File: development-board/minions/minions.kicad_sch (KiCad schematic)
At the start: 101 parts, among them J1 Pinout, J2 SWD_JLINK, J3 0.91 OLED, J4 BatCon, J5 Pinout, K1 KEYSW, K2 KEYSW, K3 KEYSW, K4 KEYSW, K5 KEYSW, K6 KEYSW, K7 KEYSW, K8 KEYSW, P1 USB_C_Plug_USB2.0, Q1 PJA3404_(G1,D3,S2), Q2 PJA3405_(G1,D3,S2), SW1 RST, SW3 PWR_SWITCH, SW4 5V_EN, U10 MAX17048, U4 CH340C, U5 BQ24075RGT_DPPM, U6 TPS63002_SEPIC_5V, U7 nRF52832-QFxx, U8 MCP23017_SS, U9 TPS63001_SEPIC_3V3, Y1 32MHz_CF4032M00020001

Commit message: feat: routing minions part 1
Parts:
- removed J4: BatCon, Connector_PinHeader_2.54mm:PinHeader_1x02_P2.54mm_Horizontal, symbol Connector_Generic:Conn_01x02
- added C10: 1uF, Capacitor_SMD:C_0805_2012Metric_Pad1.18x1.45mm_HandSolder, symbol Device:C
- added C22: 0.1uF, Capacitor_SMD:C_0805_2012Metric_Pad1.18x1.45mm_HandSolder, symbol Device:C
- added J6: ConnBattery, Connector_PinHeader_2.54mm:PinHeader_1x03_P2.54mm_Horizontal, symbol Connector_Generic:Conn_01x03
- added SW2: SW_RGB, Button_Switch_SMD:SW_SPDT_PCM12, symbol Switch:SW_Push_SPDT
- added U1: SN74LV1T34DBV, Package_TO_SOT_SMD:SOT-23-5_HandSoldering, symbol Logic_LevelTranslator:SN74LV1T34DBV
- R15, R17: value 1K -> 1K5
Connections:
- net P0.24 is gone; now on net ~{PGOOD}: J1.1 (Pin_1), U7.29 (P0.24)
- net P0.25 is gone; now on net ~{CHG}: J1.2 (Pin_2), U7.37 (P0.25)
- net P0.26 is gone; now on net ~{ALRT}: J1.3 (Pin_3), U7.38 (P0.26)
- net +5V: now also SW2.1 (A); no longer C41.1, C42.1, C43.1, C44.1, D11.4 (VDD), D17.4 (VDD), D23.4 (VDD), D8.4 (VDD)
- net +BATT: now also C22.1, J6.1 (Pin_1)
- net GND: now also C10.2, C22.2, J6.3 (Pin_3), U1.3 (GND)
- net TX: now also U1.2 (A); no longer D8.3 (DIN)
- net VBUS: now also C10.1
- net TS: now reaches U5.1 (TS)
- net TS: now also J6.2 (Pin_2)
- net ~{PGOOD}: now reaches D4.1 (K), U5.7 (~{PGOOD})
- net ~{CHG}: now reaches D32.1 (K), U5.9 (~{CHG})
- net ~{ALRT}: now reaches U10.5 (~{ALRT})
- new net: C41.1, C42.1, C43.1, C44.1, D11.4 (VDD), D17.4 (VDD), D23.4 (VDD), D8.4 (VDD), SW2.2 (B), U1.5 (VCC)
- new net: D8.3 (DIN), U1.4 (Y)
- no-connect marks 29 -> 28
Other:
- note added: "dynamic power path management"
- moved on the sheet: C1, C11, C12, C13, C14, C15, C16, C17, C2, C3, C4, C41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

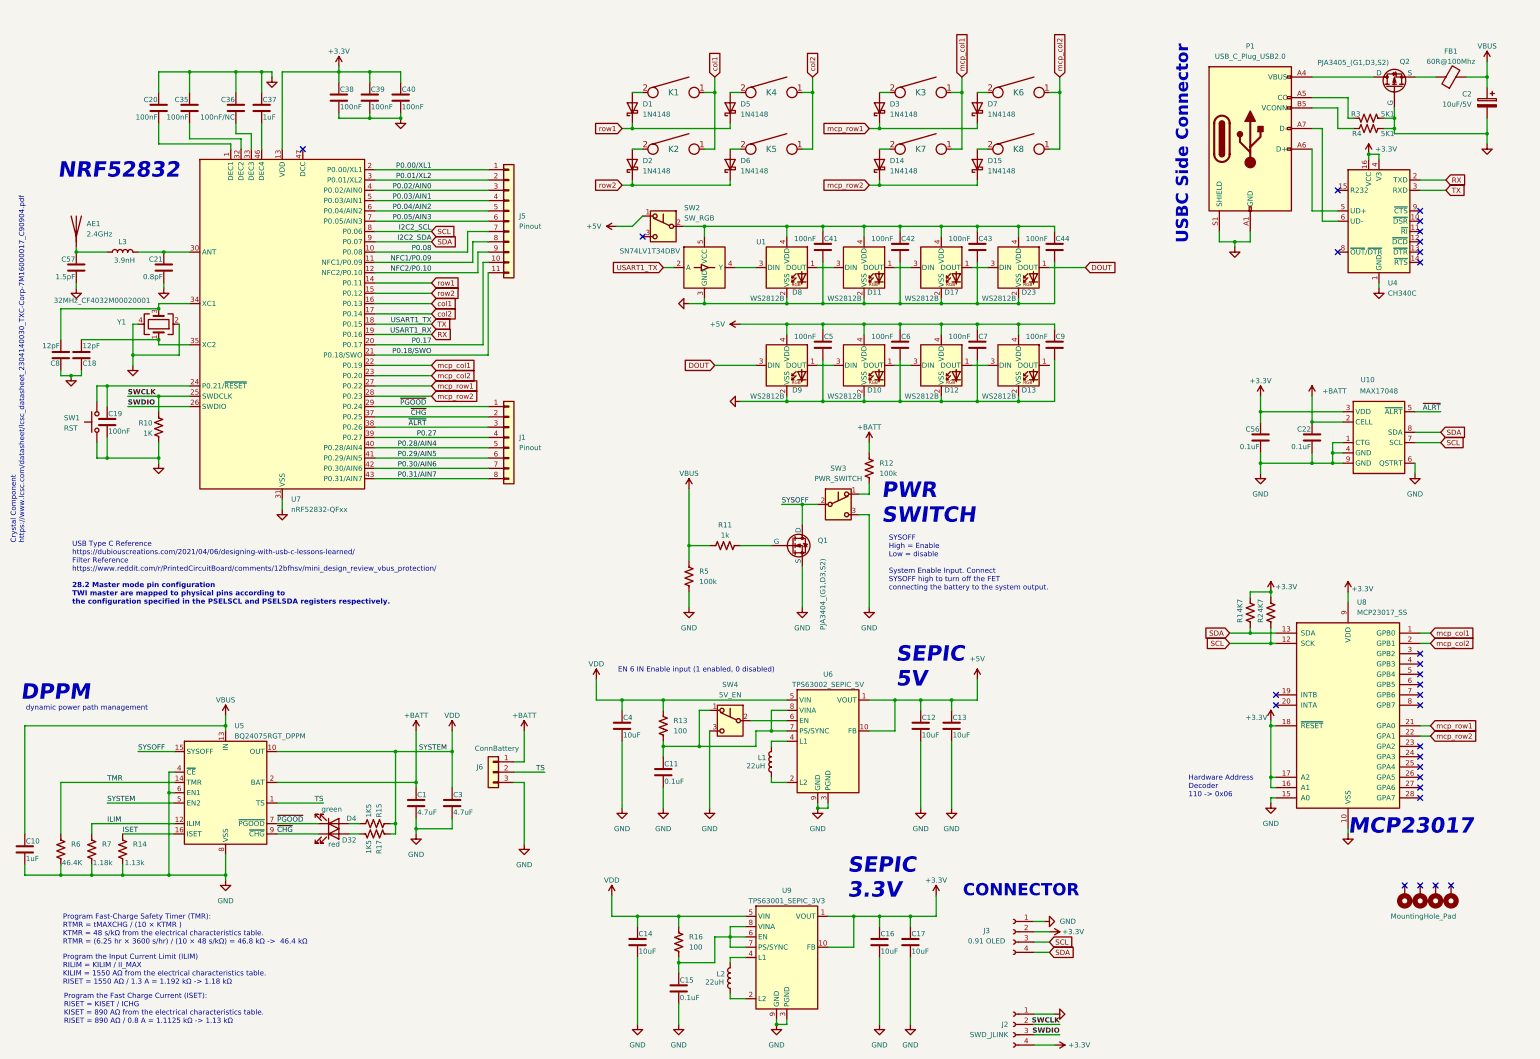
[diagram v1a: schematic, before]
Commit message: feat: finish routing part 1
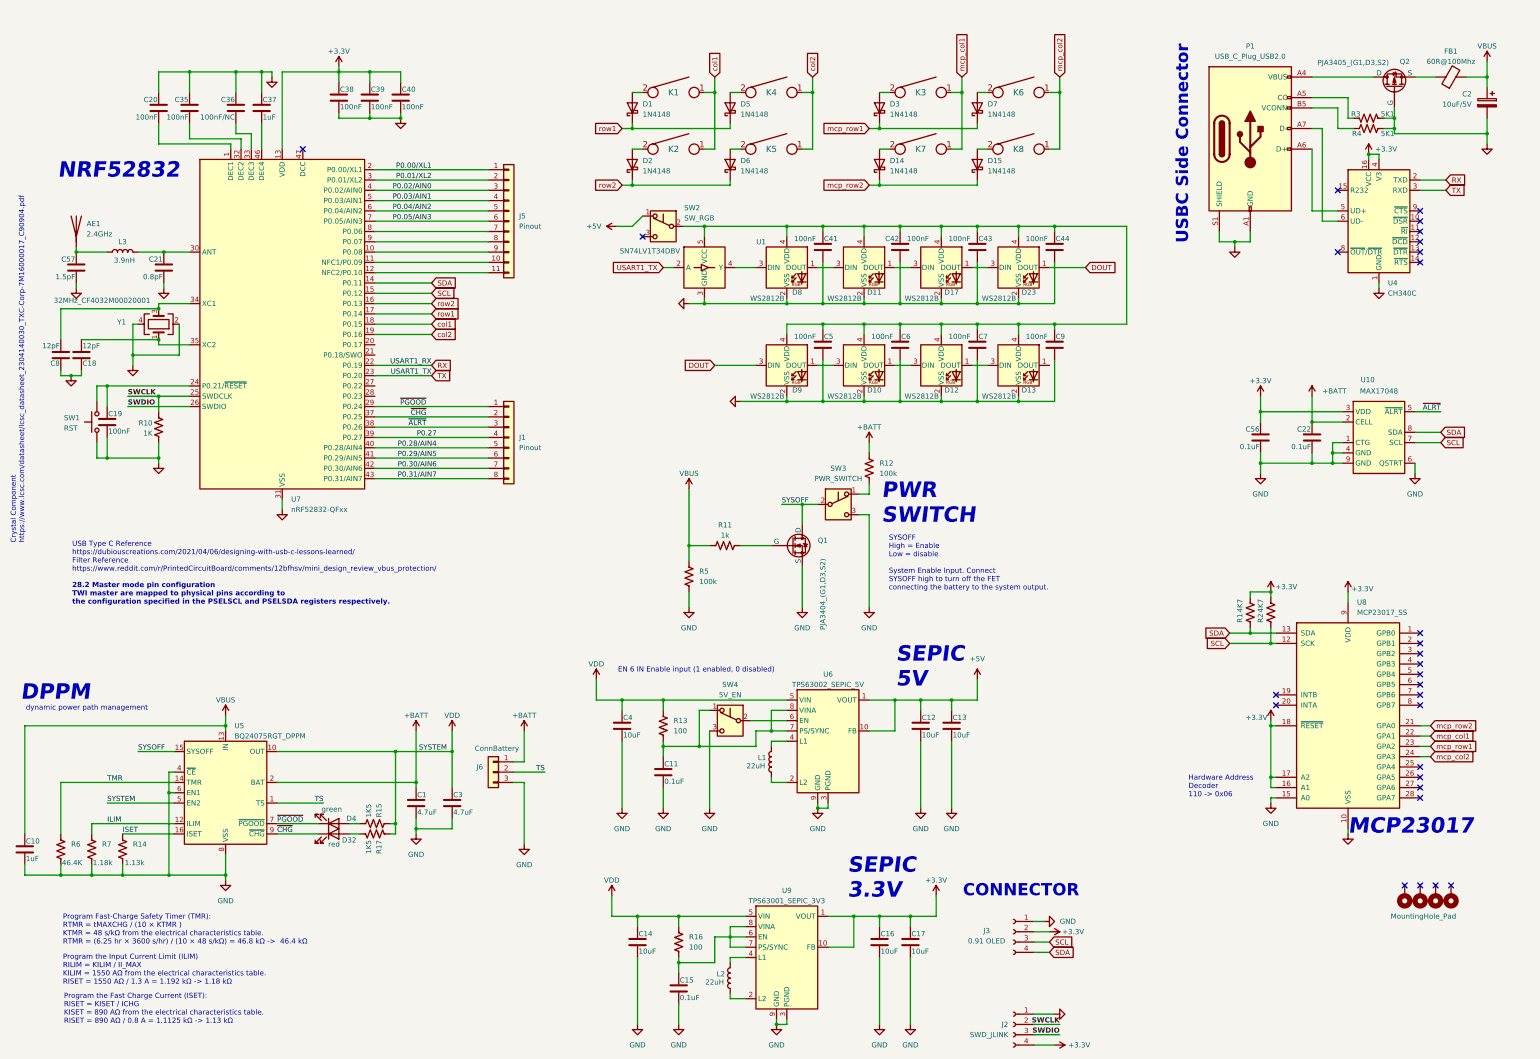
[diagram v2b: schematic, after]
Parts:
- J2: footprint Connector_PinHeader_2.54mm:PinHeader_1x04_P2.54mm_Horizontal -> Connector_PinHeader_2.54mm:PinHeader_1x04_P2.54mm_Vertical
- J6: footprint Connector_PinHeader_2.54mm:PinHeader_1x03_P2.54mm_Horizontal -> Connector_PinHeader_2.54mm:PinHeader_1x03_P2.54mm_Vertical
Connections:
- net +5V: no longer C5.1, C6.1, C7.1, C9.1, D10.4 (VDD), D12.4 (VDD), D13.4 (VDD), D9.4 (VDD)
- net RX: now also U7.22 (P0.19); no longer U7.19 (P0.16)
- net SCL: now also U7.15 (P0.12); no longer U7.8 (P0.06)
- net SDA: now also U7.14 (P0.11); no longer U7.9 (P0.07)
- net TX: now also U7.23 (P0.20); no longer U7.18 (P0.15)
- net col1: now also U7.18 (P0.15); no longer U7.16 (P0.13)
- net col2: now also U7.19 (P0.16); no longer U7.17 (P0.14)
- net mcp_col1: now also U8.22 (GPA1); no longer U7.22 (P0.19), U8.1 (GPB0)
- net mcp_col2: now also U8.24 (GPA3); no longer U7.23 (P0.20), U8.2 (GPB1)
- net mcp_row1: now also U8.23 (GPA2); no longer U7.27 (P0.22), U8.21 (GPA0)
- net mcp_row2: now also U8.21 (GPA0); no longer U7.28 (P0.23), U8.22 (GPA1)
- net row1: now also U7.17 (P0.14); no longer U7.14 (P0.11)
- net row2: now also U7.16 (P0.13); no longer U7.15 (P0.12)
- net at C41.1, C42.1, C43.1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: now also C5.1, C6.1, C7.1, C9.1, D10.4 (VDD), D12.4 (VDD), D13.4 (VDD), D9.4 (VDD)
- net NFC1/P0.09: no longer names the net of U7.11 (NFC1/P0.09)
- net NFC1/P0.09: now also J5.10 (Pin_10); no longer J5.8 (Pin_8)
- net NFC2/P0.10: no longer names the net of J5.9 (Pin_9)
- net NFC2/P0.10: now also U7.10 (P0.08); no longer U7.12 (NFC2/P0.10)
- net P0.08: no longer names the net of J5.7 (Pin_7)
- net P0.08: now also U7.8 (P0.06); no longer U7.10 (P0.08)
- net P0.17: no longer names the net of U7.20 (P0.17)
- net P0.17: no longer J5.10 (Pin_10)
- net P0.18/SWO: no longer names the net of J5.11 (Pin_11)
- net P0.18/SWO: now also U7.12 (NFC2/P0.10); no longer U7.21 (P0.18/SWO)
- new net: J5.8 (Pin_8), U7.9 (P0.07)
